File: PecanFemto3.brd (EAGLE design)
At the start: 16.6 x 21.2 mm, 35 parts, among them Q1 AP2301, U1 TPS62203DBVT

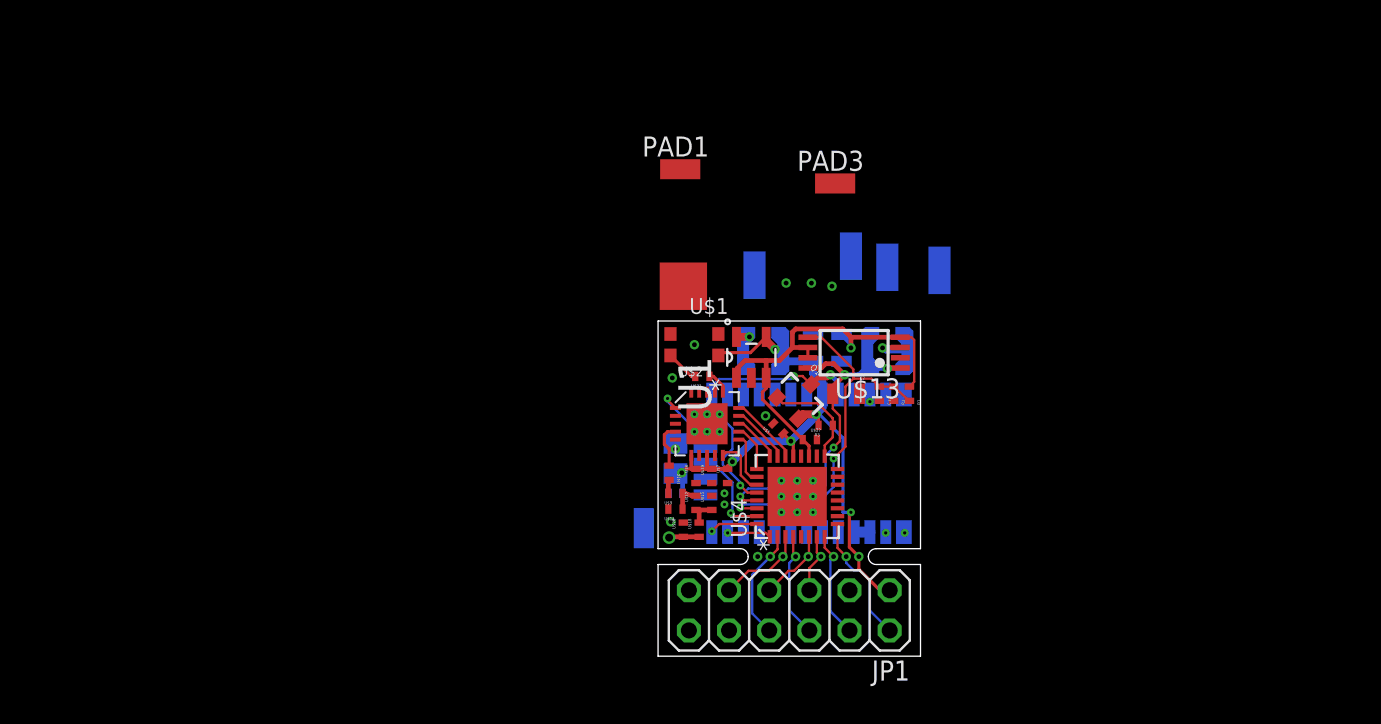
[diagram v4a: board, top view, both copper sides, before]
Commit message: Moved all parts around
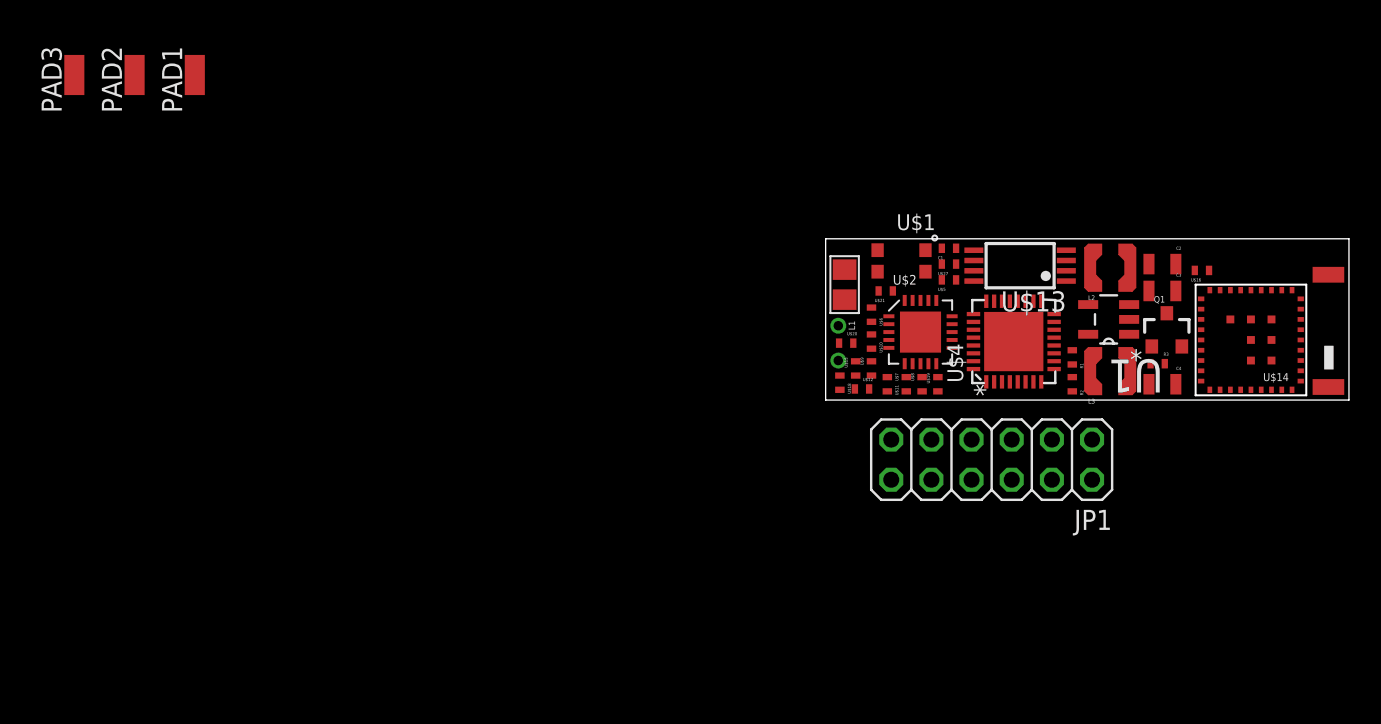
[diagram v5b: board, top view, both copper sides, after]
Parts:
- added U$14: EVA7M, eva7m:EVA7M
- added U$16: 100nF, sven:0402
- U$3: value UBLOX_CAM -> JTI_ANTENNA-1575AT43A40; device Ava:UBLOX_CAM-M8 -> Ava:JTI_ANTENNA-1575AT43A40
- moved PAD3 48.6 mm to (-33.0, 35.6), turned to 0 degrees
- moved PAD2 43.1 mm to (-29.2, 35.6), flipped to the top, turned to 0 degrees
- moved PAD1 31.3 mm to (-25.4, 35.6), turned to 0 degrees
- moved U$3 27.0 mm to (46.3, 19.0), flipped to the top, turned to 90 degrees
- moved Q1 23.7 mm to (36.1, 19.4), turned to 0 degrees
- moved U1 22.7 mm to (32.4, 20.1), turned to 180 degrees
- moved C4 22.2 mm to (35.8, 16.0), flipped to the top, turned to 180 degrees
- moved L3 22.0 mm to (32.5, 16.8), flipped to the top, turned to 0 degrees
- moved C2 21.6 mm to (35.8, 23.6)
- moved R3 21.4 mm to (35.5, 17.3), turned to 180 degrees
- moved C3 20.6 mm to (35.8, 21.9), flipped to the top, turned to 180 degrees
- moved U$4 16.8 mm to (26.4, 18.7)
- moved U$6 16.8 mm to (17.4, 20.4), flipped to the top, turned to 90 degrees
- moved JP1 16.0 mm to (25.0, 11.2)
- moved U$20 15.7 mm to (15.8, 18.6), turned to 180 degrees
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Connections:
- removed net 23/RESET_N: U$3.23/RESET_N
- removed net N$11: U$3.16/ANT, U$3.17/RF_IN
- removed net TIMEPULSE: U$3.29/TIMEPULSE, U$4.31
- new net N$1: U$14.P$1, U$3.FEED
- net CS_RADIO: now also U$4.23, U$4.25; no longer U$4.22
- net GND: now also U$14.P$18, U$14.P$2, U$16.P$2; no longer U$3.10/GND, U$3.11/GND, U$3.12/GND, U$3.13/GND, U$3.14/GND, U$3.15/GND, U$3.18/GND, U$3.19/GND, U$3.20/DSEL, U$3.21/GND, U$3.22/GND, U$3.27/GND, U$3.31/GND, U$3.4/GND, U$3.5/GND
- net GPIO1: now also U$4.1, U$4.30; no longer U$4.27
- net IRQ: now also U$4.29; no longer U$4.26
- net MISO: now also U$4.27; no longer U$4.24
- net MOSI: now also U$4.24, U$4.26; no longer U$4.23
- net N$16: now also U$14.P$19, U$14.P$20, U$16.P$1; no longer U$3.1/VCC_IO, U$3.9/VCC
- net RADIO_SDN: no longer U$4.28
- net RXD: now also U$14.P$15; no longer U$3.26/RXD, U$4.32
- net SCK: now also U$4.28; no longer U$4.25
- net TXD: now also U$14.P$16; no longer U$3.25/TXD, U$4.1
- net VBAT_DIFF: now also U$4.32; no longer U$4.30
- net VCC: now also U$14.P$21; no longer U$3.8/V_BCKP
- net VSOLAR: now also U$4.31; no longer U$4.29
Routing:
- net VCC: track 47.8 -> 0.00 mm, vias 7 -> 0
- net VBAT: track 27.6 -> 0.00 mm, vias 1 -> 0
- net VSOLAR: track 26.2 -> 0.00 mm, vias 4 -> 0
- net VBAT_DIFF: track 23.3 -> 0.00 mm, vias 2 -> 0
- net RADIO_SDN: track 11.4 -> 0.00 mm, vias 2 -> 0
- net N$16: track 10.2 -> 0.00 mm, vias 2 -> 0
- net OUT5: track 8.33 -> 0.00 mm, vias 1 -> 0
- net OUT2: track 7.03 -> 0.00 mm, vias 1 -> 0
- net N$14: track 6.98 -> 0.00 mm, vias 1 -> 0
- net OUT4: track 6.74 -> 0.00 mm, vias 1 -> 0
- net GPS_OFF: track 6.68 -> 0.00 mm
- net OUT3: track 6.67 -> 0.00 mm, vias 1 -> 0
- net N$15: track 6.66 -> 0.00 mm, vias 1 -> 0
- net TIMEPULSE: track 5.92 -> 0.00 mm, vias 1 -> 0
- net RESET: track 5.61 -> 0.00 mm, vias 1 -> 0
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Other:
- board size 16.6 x 21.2 mm -> 33.1 x 10.2 mm
- board text removed: "GND"
- board text removed: "VBAT"
- board text removed: "VSOLAR & GND"

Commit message: Removed GPS-Switch-MOSFET and connected parts
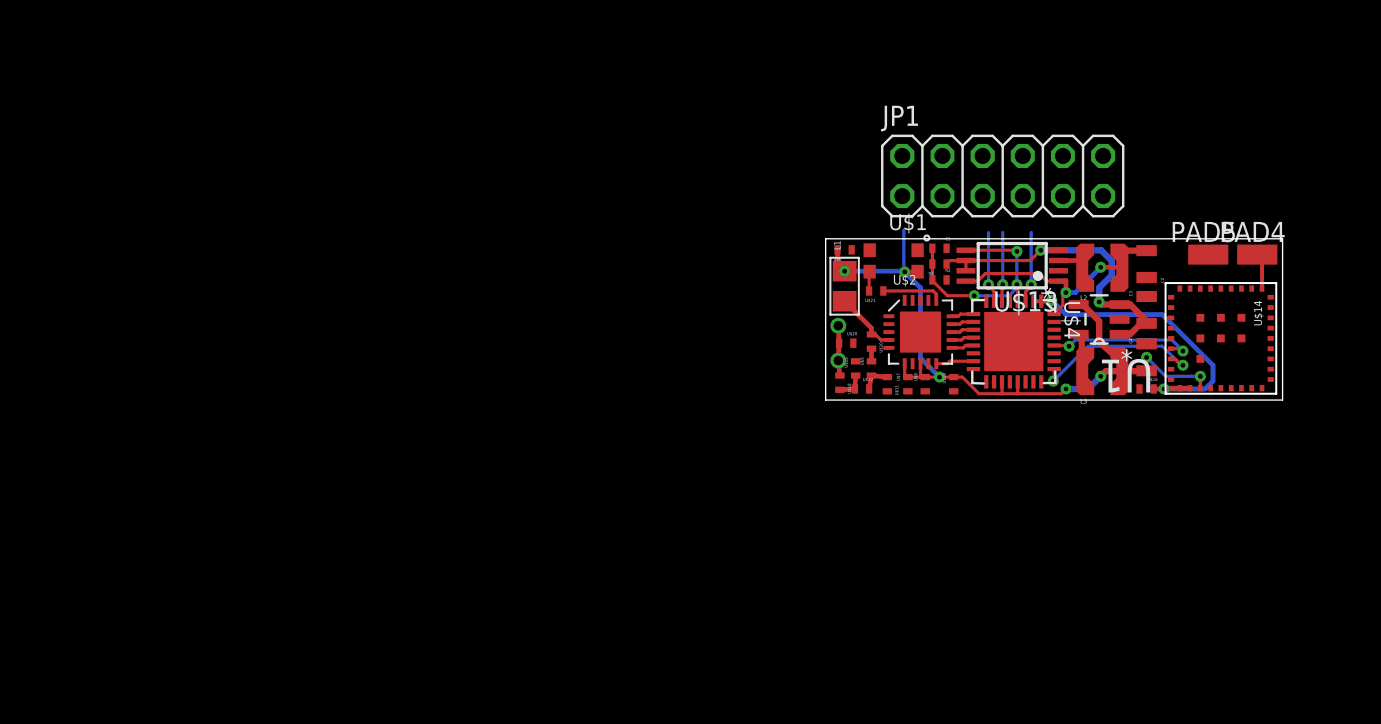
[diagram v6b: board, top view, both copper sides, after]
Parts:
- removed PAD1, PAD2, PAD3: (no value), PecanFemto4:SMD1,27-2,54
- removed Q1: AP2301, PecanPico6:SOT23-3
- removed R3: 47k, PecanPico6:0402
- removed U$27, U$5: 100nF, sven:0402
- removed U$3: JTI_ANTENNA-1575AT43A40, Ava:JTI_ANTENNA-1575AT43A40
- added PAD4, PAD5: (no value), PecanFemto4:SMD1,27-2,54
- moved JP1 18.0 mm to (25.7, 29.2), turned to 0 degrees
- moved R2 10.7 mm to (21.7, 22.6), turned to 180 degrees
- moved R1 10.3 mm to (21.7, 23.6), turned to 0 degrees
- moved U$16 8.28 mm to (34.8, 15.7), turned to 180 degrees
- moved U$6 4.44 mm to (15.7, 24.5), turned to 0 degrees
- moved C4 1.97 mm to (34.8, 17.7), turned to 270 degrees
- moved U$14 1.90 mm to (39.5, 18.9), turned to 270 degrees
- moved C3 1.56 mm to (34.8, 20.7), turned to 270 degrees
- moved C2 1.00 mm to (34.8, 23.6), turned to 90 degrees
- moved U$19 1.00 mm to (22.6, 16.0)
- moved C1 0.60 mm to (21.7, 24.6), turned to 180 degrees
- moved U$21 0.60 mm to (17.7, 21.9)
- moved U1 0.60 mm to (31.8, 20.1)
- moved L2 0.50 mm to (32.0, 23.4)
- moved L3 0.50 mm to (32.0, 16.8)
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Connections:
- removed net GPS_OFF: Q1.1, R3.P$2, U$4.17
- removed net N$16: Q1.3, U$14.P$19, U$14.P$20, U$16.P$1
- new net VCC_GPS: U$14.P$19, U$14.P$20, U$16.P$1, U$4.1, U$4.2
- net CS_RADIO: now also U$4.9; no longer U$4.23, U$4.25
- net GND: now also PAD5.1; no longer PAD1.1, PAD3.1, U$27.P$1, U$5.P$1
- net GPIO1: now also U$4.15; no longer U$4.1, U$4.30
- net IRQ: now also U$4.13; no longer U$4.29
- net MISO: now also U$4.11; no longer U$4.27
- net MOSI: now also U$4.10; no longer U$4.24, U$4.26
- net N$1: now also PAD4.1; no longer U$3.FEED
- net N$3: no longer PAD2.1
- net OUT2: no longer U$4.2
- net OUT3: no longer U$4.4
- net OUT4: no longer U$4.8
- net OUT5: no longer U$4.9
- net RXD: now also U$4.28
- net SCK: now also U$4.12; no longer U$4.28
- net TXD: now also U$4.25
- net VBAT: no longer U$27.P$2, U$4.19
- net VBAT_DIFF: now also U$4.4; no longer U$4.32
- net VCC: now also U$4.19; no longer Q1.2, R3.P$1, U$5.P$2
- net VSOLAR: now also U$4.32; no longer U$4.31
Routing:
- net VCC: track 0.00 -> 50.1 mm, vias 0 -> 7
- net VBAT: track 0.00 -> 21.4 mm, vias 0 -> 2
- net VCC_GPS: track 0.00 -> 19.7 mm, vias 0 -> 2
- net VSOLAR: track 0.00 -> 19.2 mm, vias 0 -> 2
- net VBAT_DIFF: track 0.00 -> 14.6 mm, vias 0 -> 3
- net TXD: track 0.00 -> 11.3 mm, vias 0 -> 2
- net RXD: track 0.00 -> 9.44 mm, vias 0 -> 2
- net N$15: track 0.00 -> 6.31 mm
- net N$14: track 0.00 -> 5.78 mm
- net RESET: track 0.00 -> 4.50 mm, vias 0 -> 1
- net SWDIO: track 0.00 -> 4.47 mm, vias 0 -> 1
- net SWCLK: track 0.00 -> 4.37 mm, vias 0 -> 1
- net N$2: track 0.00 -> 4.05 mm
- net N$10: track 0.00 -> 3.83 mm
- net N$3: track 0.00 -> 3.16 mm
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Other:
- board size 33.1 x 10.2 mm -> 28.9 x 10.2 mm

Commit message: Routed parts
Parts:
- moved U$4 0.10 mm to (26.5, 18.7)
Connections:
- net RXD: now also U$4.24; no longer U$4.28
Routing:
- net GND: track 0.00 -> 4.74 mm, vias 0 -> 26
- net VCC_GPS: track 19.7 -> 17.8 mm
- net RXD: track 9.44 -> 11.1 mm
- net TXD: track 11.3 -> 10.4 mm
- added copper zone on layer 1, net GND
- added copper zone on layer 16, net GND

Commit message: Updated libraries, moved parts around, routed
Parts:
- added ANTENNA, GND, GND15, VBAT: (no value), PecanFemto4:SMD1,27-2,54
- added IC4: SI4060/3, PecanFemto4:QFN-20
- added TCXO: TXC 7Z-26.000MCG-T, tcxo:TCXO_2.0X1.6
- IC1: value SPV1040 -> SPV1040T
- L2: value 33uH -> LPS3015-103MRB
- L3: value 10uH -> LPS3015-103MRB
- U$1: value 3.2X2.5-TCXO -> 100nF; device Ava:3.2X2.5-TCXO -> sven:0402
- U$2: value SI4060/3 -> 100pF; device PecanFemto4:QFN-20 -> sven:0402
- moved U$21 4.44 mm to (22.1, 22.5), turned to 270 degrees
- moved U$2 3.26 mm to (21.1, 22.5), turned to 270 degrees
- moved R2 2.69 mm to (19.8, 24.5), turned to 0 degrees
- moved L1 2.08 mm to (16.9, 20.5)
- moved U$6 1.66 mm to (16.4, 23.0), turned to 90 degrees
- moved U$1 1.61 mm to (17.4, 23.0), turned to 270 degrees
- moved U$20 1.21 mm to (15.3, 19.7), turned to 270 degrees
- moved U$18 1.00 mm to (15.3, 17.1)
- moved U$9 1.00 mm to (17.4, 16.0)
- moved U$12 0.90 mm to (15.9, 15.7)
- moved U$10 0.80 mm to (17.4, 17.9)
- moved C1 0.72 mm to (21.1, 24.2), turned to 90 degrees
- moved R1 0.72 mm to (22.1, 24.2), turned to 270 degrees
- moved L3 0.20 mm to (31.8, 16.8)
- moved U$15 0.14 mm to (16.3, 17.1)
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- renumbered U$13 to IC1, U$14 to IC3, U$4 to IC5
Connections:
- removed net OUT5: JP1.2
- new net N$7: IC4.17, U$2.P$2
- new net OUT1: IC5.5, JP1.8
- net CS_RADIO: now also IC4.15; no longer U$2.15
- net GND: now also GND.1, GND15.1, IC3.P$37, IC3.P$38, IC3.P$39, IC3.P$40, IC3.P$41, IC3.P$42, IC3.P$43, IC4.18, IC4.21, TCXO.1, TCXO.2, U$1.P$1; no longer U$1.1, U$1.2, U$2.18, U$2.21
- net GPIO1: now also IC4.10, IC5.16; no longer IC5.15, U$2.10
- net IRQ: now also IC4.11; no longer U$2.11
- net MISO: now also IC4.13; no longer U$2.13
- net MOSI: now also IC4.14; no longer U$2.14
- net N$10: now also IC4.16; no longer U$2.16
- net N$2: now also IC4.4; no longer U$2.4
- net N$3: now also ANTENNA.1
- net N$9: now also TCXO.3, U$2.P$1; no longer U$1.3
- net OUT2: now also IC5.8, JP1.6; no longer JP1.8
- net OUT3: now also JP1.4; no longer JP1.6
- net OUT4: now also JP1.2; no longer JP1.4
- net RADIO_SDN: now also IC4.1; no longer U$2.1
- net RXD: now also IC5.25; no longer IC5.24
- net SCK: now also IC4.12; no longer U$2.12
- net TXD: now also IC5.24; no longer IC5.25
- net VBAT: now also VBAT.1
- net VCC: now also IC4.6, IC4.8, TCXO.4, U$1.P$2; no longer U$1.4, U$2.6, U$2.8
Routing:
- net VBAT_DIFF: track 14.9 -> 9.82 mm, vias 3 -> 2
- net OUT2: track 0.00 -> 4.69 mm
- net OUT1: track 0.00 -> 4.57 mm
- net N$10: track 3.97 -> 1.12 mm
- net VCC_GPS: track 17.8 -> 15.5 mm, vias 2 -> 4
- net N$3: track 3.16 -> 1.70 mm, vias 2 -> 0
- net N$2: track 4.05 -> 2.61 mm
- net RXD: track 11.1 -> 9.82 mm
- net N$9: track 1.23 -> 2.20 mm
- net VCC: track 50.2 -> 51.1 mm, vias 7 -> 5
- net N$7: track 0.00 -> 0.85 mm
- net VBAT: track 21.4 -> 22.2 mm, vias 2 -> 3
- net N$15: track 6.31 -> 5.77 mm
- net VSOLAR: track 19.2 -> 19.6 mm, vias 2 -> 4
- net SWCLK: track 4.38 -> 4.61 mm, vias 1 -> 0
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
